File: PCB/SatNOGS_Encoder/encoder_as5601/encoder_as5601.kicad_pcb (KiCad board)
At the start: 2 copper layers, 25 x 22.5 mm, 8 parts, among them P1 CONN_02X05, Q1 Q_NMOS_GSD, U1 AS5601

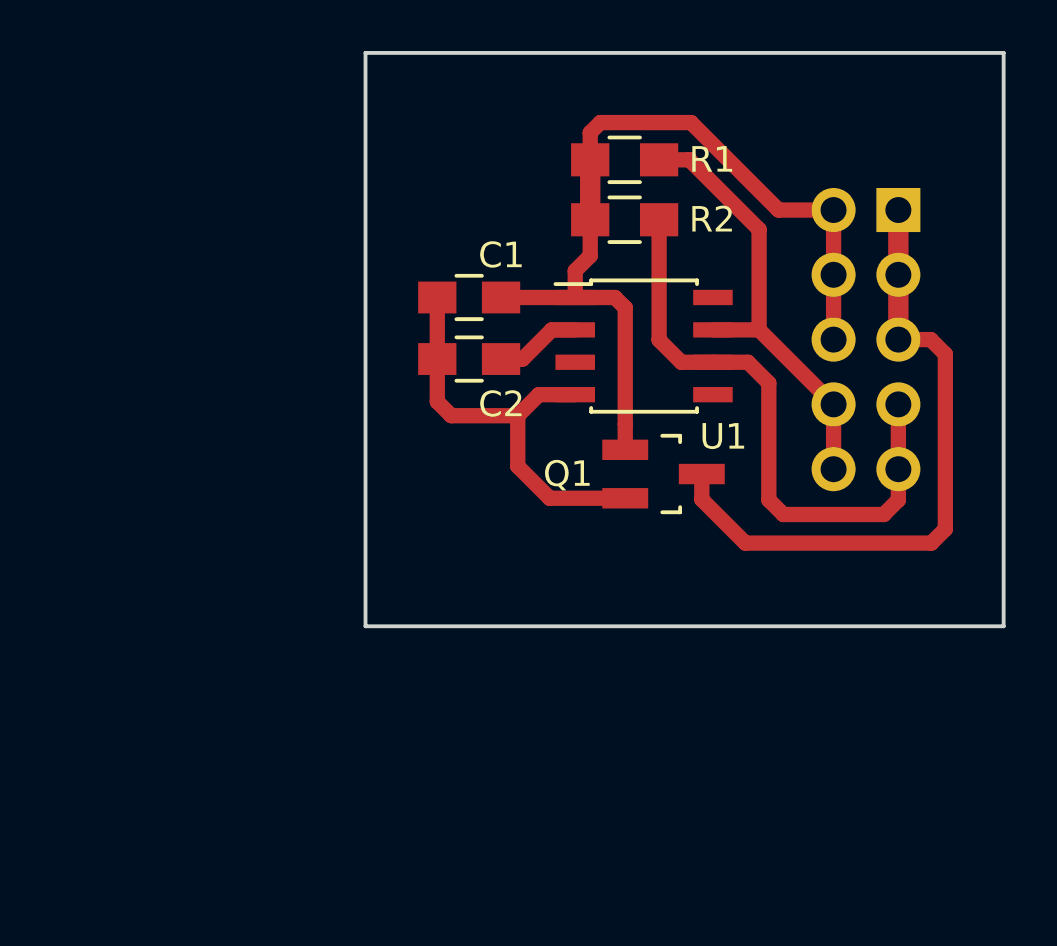
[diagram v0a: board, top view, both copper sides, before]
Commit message: Encoder case (#19)
* Update pcb to mount in cas.

Add mount holes.
Rearraange parts in order to place the AS5601 in the middle of PCB.

* Silksreen fixes.
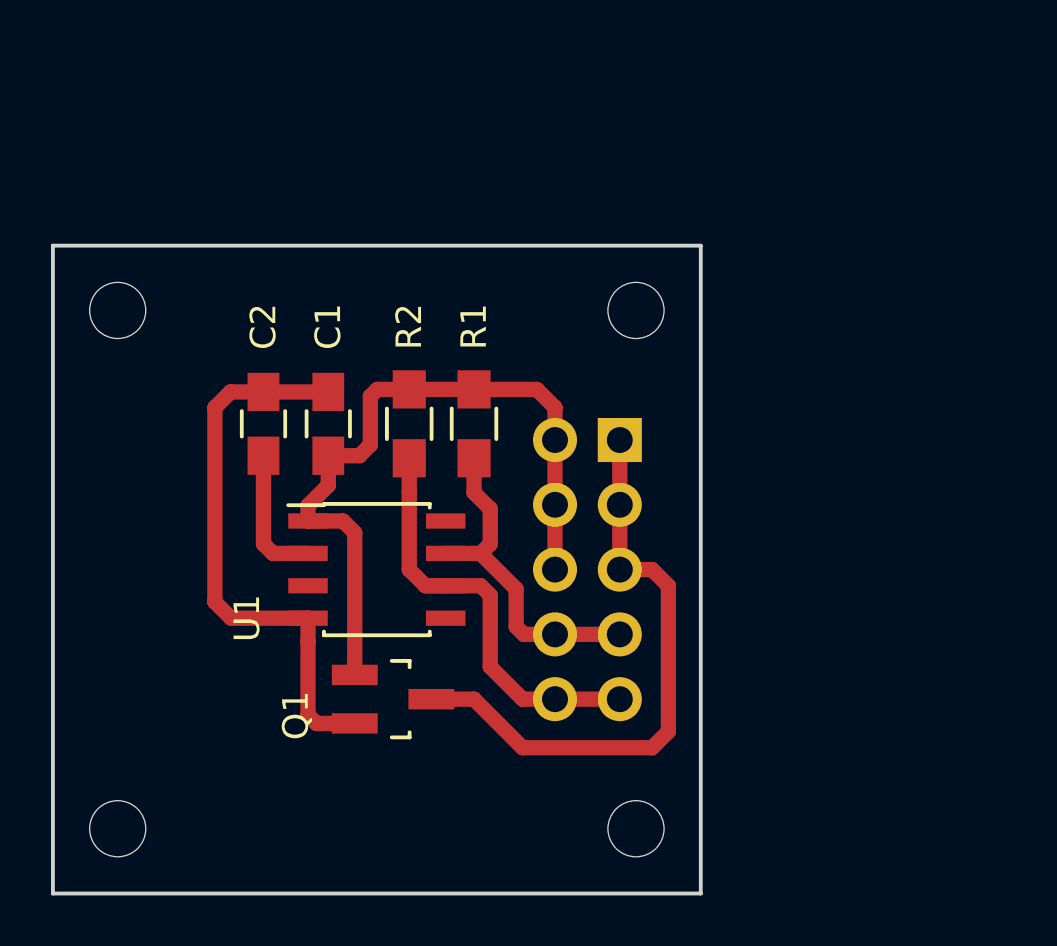
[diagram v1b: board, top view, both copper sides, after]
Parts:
- removed SatNOGS_Encoder: ©2016 Libre Space Foundation, Symbols:Symbol_OSHW-Logo_SilkScreen
- added REF**: MountingHole_2.2mm_M2, Mounting_Holes:MountingHole_2.2mm_M2, F.Cu at (123.2, 78.7)
- added REF**: MountingHole_2.2mm_M2, Mounting_Holes:MountingHole_2.2mm_M2, F.Cu at (123.2, 99.1)
- added REF**: MountingHole_2.2mm_M2, Mounting_Holes:MountingHole_2.2mm_M2, F.Cu at (143.5, 78.7)
- added REF**: MountingHole_2.2mm_M2, Mounting_Holes:MountingHole_2.2mm_M2, F.Cu at (143.5, 99.1)
- added ©2016 LSF: SatNOGS-Encoder, Symbols:OSHW-Logo2_7.3x6mm_SilkScreen, B.Cu at (128.9, 92.7)
- moved P1 14.2 mm to (142.9, 83.8)
- moved Q1 13.8 mm to (134.0, 94.0)
- moved U1 13.7 mm to (133.3, 88.9)
- moved R1 11.9 mm to (137.2, 83.2), turned to 270 degrees
- moved R2 11.6 mm to (134.6, 83.2), turned to 270 degrees
- moved C2 8.46 mm to (128.9, 83.2), turned to 90 degrees
- moved C1 7.42 mm to (131.4, 83.2), turned to 90 degrees
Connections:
- P1 pad 10: /SCL -> /SDA
- P1 pad 7: /SDA -> /SCL
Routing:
- net /SDA: track 23.6 -> 16.4 mm
- net +5V: track 33.5 -> 28.2 mm
- net GND: track 16.8 -> 22.0 mm
- net /SCL: track 17.5 -> 13.2 mm
- net Net-(P1-Pad1): track 25.5 -> 23.3 mm
- net Net-(C2-Pad1): track 3.38 -> 5.36 mm
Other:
- board size 25 x 22.5 mm -> 25.4 x 25.4 mm
- net class power added: clearance 0.2, trace_width 0.6, via_dia 0.8, via_drill 0.4
- net class signals added: clearance 0.2, trace_width 0.6, via_dia 0.8, via_drill 0.4
- board text added: "SCL"
- board text added: "SDA"
- board text removed: "SDA|SCL"
